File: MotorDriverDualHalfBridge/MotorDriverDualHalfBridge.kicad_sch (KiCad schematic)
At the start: 41 parts, among them J1 Battery Terminal +, J2 Battery Terminal -, J3 Motor Battery Connection, J4 Motor Load Connection, J5 Conn_01x02_Male, J6 Conn_01x02_Male, K1 G8PM, Q1 IAUA250N04S6N005, Q2 IAUA250N04S6N005, Q3 Q_NMOS_DGS, U1 2ED21824S06J, U2 TLI4871

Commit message: PCB V0.1
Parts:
- removed J5, J6: Conn_01x02_Male, Connector_PinHeader_1.27mm:PinHeader_1x02_P1.27mm_Vertical, symbol Connector:Conn_01x02_Male
- added C14: 100uF, Capacitor_SMD:CP_Elec_10x14.3, symbol Device:C_Polarized_Small_US
- added C16, C17, C18, C19, C20: 100uF, Capacitor_SMD:CP_Elec_6.3x5.4_Nichicon, symbol Device:C_Polarized_Small_US
- added HS1: Heatsink_Pad, Library:HSB25-282810, symbol Mechanical:Heatsink_Pad
- added J10: RJ45_LED_Shielded, Connector_RJ:RJ45_Amphenol_RJHSE538X, symbol Connector:RJ45_LED_Shielded
- added J5, J6: Conn_01x04, Connector_JST:JST_EH_B4B-EH-A_1x04_P2.50mm_Vertical, symbol Connector_Generic:Conn_01x04
- added J7: Conn_01x06_Pin, Connector_PinHeader_1.27mm:PinHeader_1x06_P1.27mm_Vertical, symbol Connector:Conn_01x06_Pin
- added NT1: NetTie_2, NetTie:NetTie-2_SMD_Pad2.0mm, symbol Device:NetTie_2
- C13, C6: footprint Capacitor_SMD:CP_Elec_5x4.4 -> Capacitor_SMD:CP_Elec_10x14.3
- F1: footprint Fuse:Fuseholder_Clip-5x20mm_Bel_FC-203-22_Lateral_P17.80x5.00mm_D1.17mm_Horizontal -> Fuse:Fuseholder_Blade_Mini_Keystone_3568
- Q1, Q2: footprint IFX-PG-HSOF-5-1-V:IFX-PG-HSOF-5-1-V -> Library:IAUA250N04S6N005AUMA1
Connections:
- net +12V: now also C20.1, J6.1 (Pin_1), J6.2 (Pin_2)
- net +3.3V: now also C19.1, J5.1 (Pin_1), J5.2 (Pin_2)
- net +BATT: now also C14.1, C16.1, C17.1, C18.1
- net A_{OUT}: now also J10.1, J7.6 (Pin_6)
- net GND: now also C19.2, C20.2, J10.10, J10.12, J10.3, J10.6, J10.SH, J5.3 (Pin_3), J5.4 (Pin_4), J6.3 (Pin_3), J6.4 (Pin_4), NT1.1; no longer C5.2, Q2.1 (S), Q2.2 (S), Q2.3 (S), Q2.4 (S)
- net GNDPWR: now also C5.2, Q2.1 (S), Q2.2 (S), Q2.3 (S), Q2.4 (S), C14.2, NT1.2
- net H_{IN}: now also J10.8, J7.1 (Pin_1)
- net LOAD: now also C16.2, C17.2, C18.2
- net L_{IN}: now also J10.7, J7.2 (Pin_2)
- net OCD_{1}: now also J10.5, J10.9, J7.3 (Pin_3)
- net OCD_{2}: now also J10.11, J10.4, J7.4 (Pin_4)
- net V_{REF}: now also J10.2, J7.5 (Pin_5)
- no-connect marks 0 -> 1
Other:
- moved on the sheet: C1, C13, C2, C3, C4, C5, J3, J4, JP1, Q1, Q2, R1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

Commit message: Updated Schematic
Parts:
- removed C14: 100uF, Capacitor_SMD:CP_Elec_10x14.3, symbol Device:C_Polarized_Small_US
- removed D1: D_TVS, Diode_SMD:D_SMF, symbol Device:D_TVS
- removed J10: RJ45_LED_Shielded, Connector_RJ:RJ45_Amphenol_RJHSE538X, symbol Connector:RJ45_LED_Shielded
- removed J7: Conn_01x06_Pin, Connector_PinHeader_1.27mm:PinHeader_1x06_P1.27mm_Vertical, symbol Connector:Conn_01x06_Pin
- removed K1: G8PM, Library:G8PM1AW7RDC12, symbol MyLibrary:G8PM
- removed Q3: Q_NMOS_DGS, Package_TO_SOT_THT:TO-220F-3_Vertical, symbol Device:Q_NMOS_DGS
- removed R8: 120Ω, Resistor_SMD:R_0603_1608Metric_Pad0.98x0.95mm_HandSolder, symbol Device:R_Small
- added J11, J7, J8: Conn_01x03, Library:MOLEX_2078430003_L1NK_250_3-PIN, symbol Connector_Generic:Conn_01x03
- J5, J6: footprint Connector_JST:JST_EH_B4B-EH-A_1x04_P2.50mm_Vertical -> Library:MOLEX_2078430004_L1NK_250_4-PIN
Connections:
- net +BATT: now also U2.7 (IP-)
- net A_{OUT}: now also J11.2 (Pin_2)
- net GND: now also J11.3 (Pin_3), J7.3 (Pin_3), J8.3 (Pin_3)
- net H_{IN}: now also J8.1 (Pin_1)
- net L_{IN}: now also J8.2 (Pin_2)
- net OCD_{1}: now also J7.1 (Pin_1)
- net OCD_{2}: now also J7.2 (Pin_2)
- net V_{REF}: now also J11.1 (Pin_1)
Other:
- moved on the sheet: C10, C11, C12, C13, C6, C7, C8, C9, F1, J1, J2, R10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

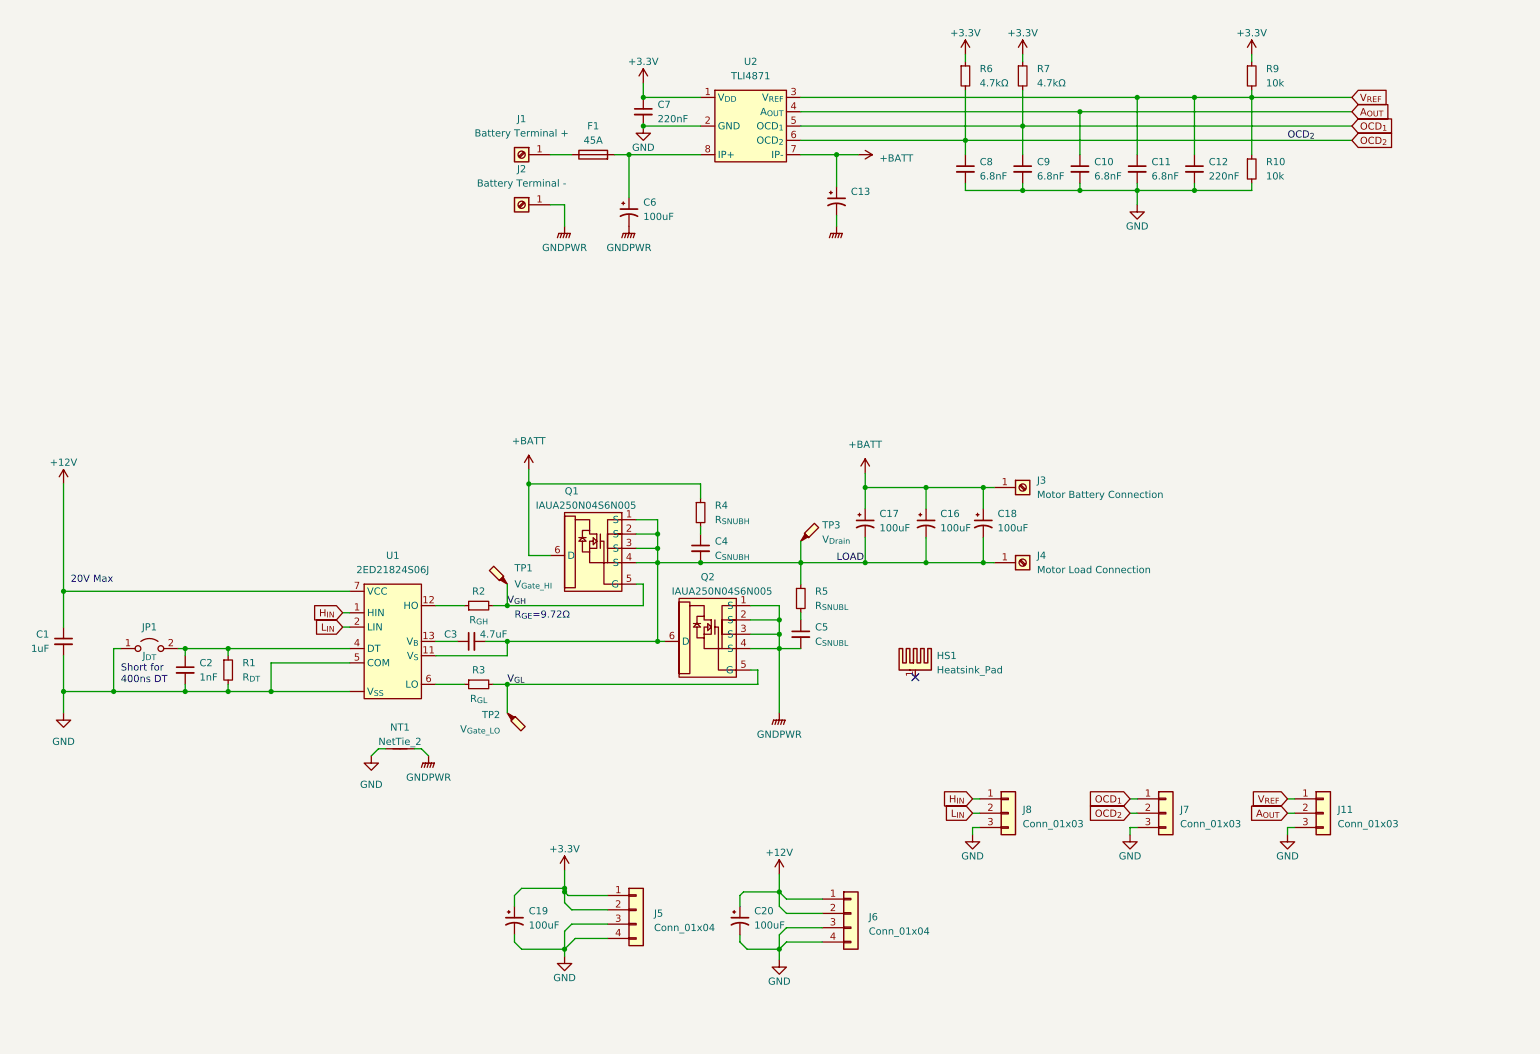
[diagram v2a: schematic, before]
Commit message: Updated Motor Driver Dual Half Bridge
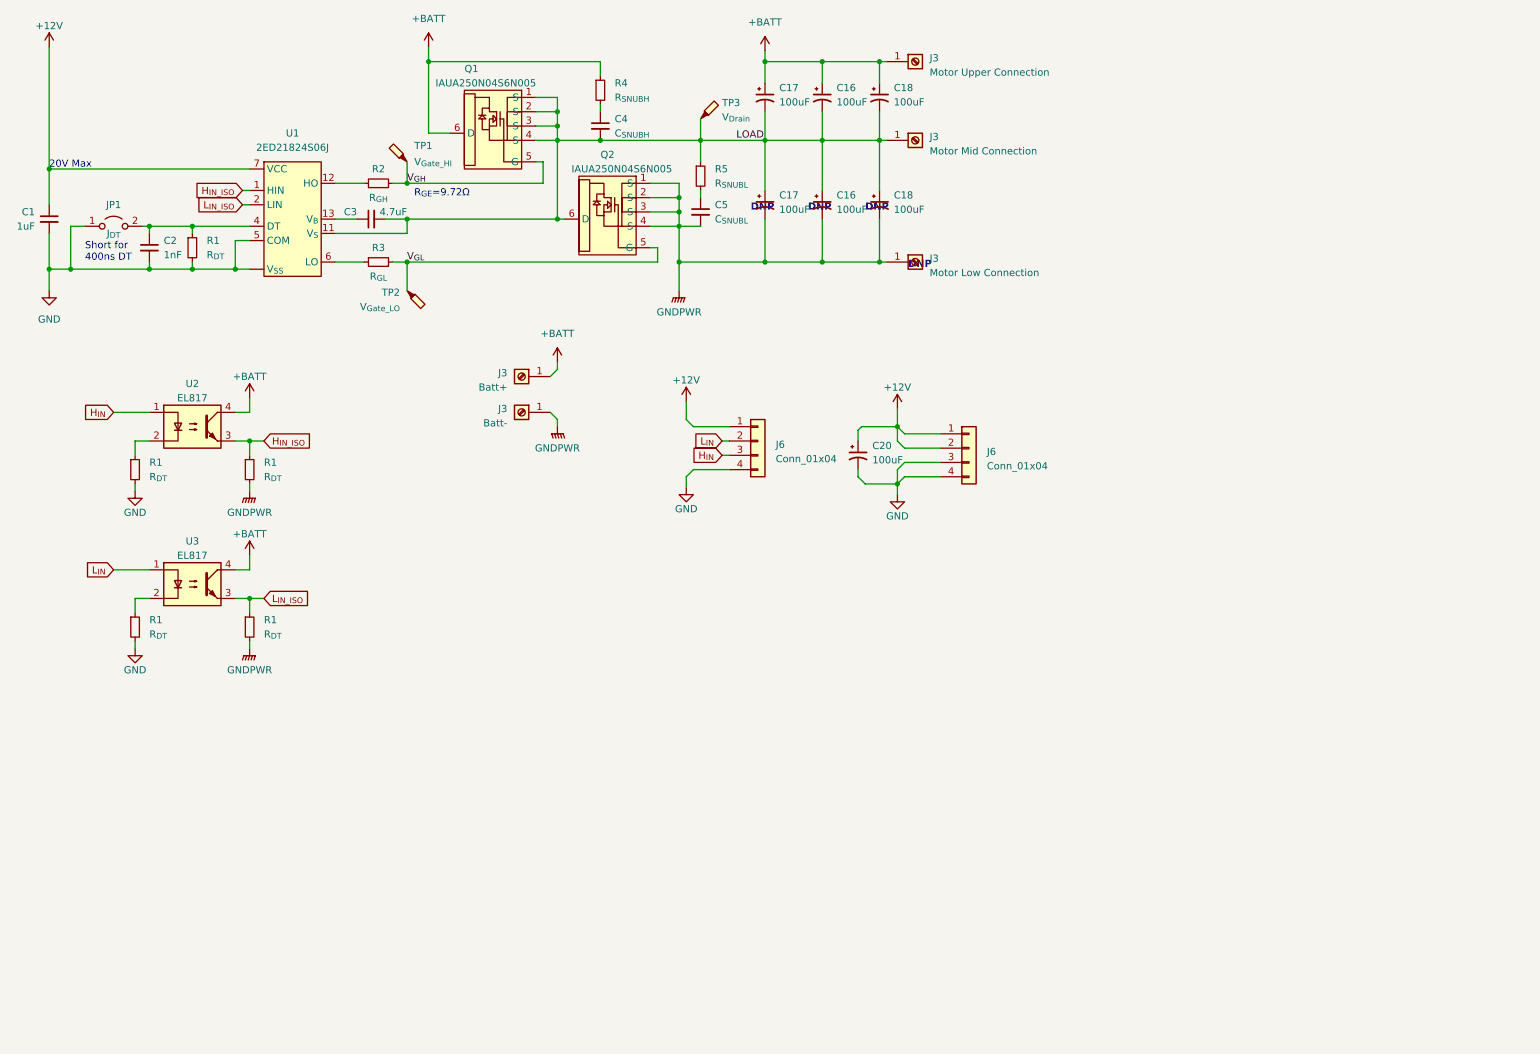
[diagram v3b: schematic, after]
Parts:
- removed C10, C11, C8, C9: 6.8nF, Capacitor_SMD:C_0603_1608Metric_Pad1.08x0.95mm_HandSolder, symbol Device:C_Small
- removed C12, C7: 220nF, Capacitor_SMD:C_0603_1608Metric_Pad1.08x0.95mm_HandSolder, symbol Device:C_Small
- removed C13, C6: 100uF, Capacitor_SMD:CP_Elec_10x14.3, symbol Device:C_Polarized_Small_US
- removed C19: 100uF, Capacitor_SMD:CP_Elec_6.3x5.4_Nichicon, symbol Device:C_Polarized_Small_US
- removed F1: 45A, Fuse:Fuseholder_Blade_Mini_Keystone_3568, symbol Device:Fuse
- removed HS1: Heatsink_Pad, Library:HSB25-282810, symbol Mechanical:Heatsink_Pad
- removed J1: Battery Terminal +, Library:74651195R, symbol Connector:Screw_Terminal_01x01
- removed J11, J7, J8: Conn_01x03, Library:MOLEX_2078430003_L1NK_250_3-PIN, symbol Connector_Generic:Conn_01x03
- removed J2: Battery Terminal -, Library:74651195R, symbol Connector:Screw_Terminal_01x01
- removed J4: Motor Load Connection, Library:74651195R, symbol Connector:Screw_Terminal_01x01
- removed J5: Conn_01x04, Library:MOLEX_2078430004_L1NK_250_4-PIN, symbol Connector_Generic:Conn_01x04
- removed NT1: NetTie_2, NetTie:NetTie-2_SMD_Pad2.0mm, symbol Device:NetTie_2
- removed R10, R9: 10k, Resistor_SMD:R_0603_1608Metric_Pad0.98x0.95mm_HandSolder, symbol Device:R_Small
- removed R6, R7: 4.7kΩ, Resistor_SMD:R_0603_1608Metric_Pad0.98x0.95mm_HandSolder, symbol Device:R_Small
- removed U2: TLI4871, Library:TLI4971A120T5E0001XUMA1, symbol MyLibrary:TLI4871
- added C16, C17, C18: 100uF, Capacitor_SMD:CP_Elec_6.3x5.4_Nichicon, symbol Device:C_Polarized_Small_US
- added J3: Batt-, TerminalBlock_Wuerth:Wuerth_REDCUBE-THR_WP-THRBU_74650194_THR, symbol Connector:Screw_Terminal_01x01
- added J3: Motor Mid Connection, TerminalBlock_Wuerth:Wuerth_REDCUBE-THR_WP-THRBU_74650194_THR, symbol Connector:Screw_Terminal_01x01
- added J3: Batt+, TerminalBlock_Wuerth:Wuerth_REDCUBE-THR_WP-THRBU_74650194_THR, symbol Connector:Screw_Terminal_01x01
- added J3: Motor Low Connection, TerminalBlock_Wuerth:Wuerth_REDCUBE-THR_WP-THRBU_74650194_THR, symbol Connector:Screw_Terminal_01x01
- added J6: Conn_01x04, Library:MOLEX_2078430004_L1NK_250_4-PIN, symbol Connector_Generic:Conn_01x04
- added R1 (x4): R_{DT}, Resistor_THT:R_Axial_DIN0207_L6.3mm_D2.5mm_P10.16mm_Horizontal, symbol Device:R_Small
- added U2, U3: EL817, Package_DIP:DIP-4_W7.62mm, symbol Isolator:EL817
- J3: value Motor Battery Connection -> Motor Upper Connection; footprint Library:74651195R -> TerminalBlock_Wuerth:Wuerth_REDCUBE-THR_WP-THRBU_74650194_THR
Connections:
- net +12V: now also J6.1 (Pin_1)
- net +BATT: now also J3.1 (Pin_1), U2.4, U3.4
- net GND: now also J6.4 (Pin_4), R1.2, R1.2
- net GNDPWR: now also C16.2, C17.2, C18.2, J3.1 (Pin_1), J3.1 (Pin_1), R1.2, R1.2
- net H_{IN}: now also J6.3 (Pin_3), U2.1; no longer U1.1 (HIN)
- net LOAD: now also C16.1, C17.1, C18.1, J3.1 (Pin_1)
- net L_{IN}: now also J6.2 (Pin_2), U3.1; no longer U1.2 (LIN)
- new net: R1.1, U2.2
- new net: R1.1, U3.2
- new net H_{IN}_{_ISO}: R1.1, U1.1 (HIN), U2.3
- new net L_{IN}_{_ISO}: R1.1, U1.2 (LIN), U3.3
- no-connect marks 1 -> 0
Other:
- note added: "DNP"
- moved on the sheet: C1, C16, C17, C18, C2, C20, C3, C4, C5, J3, J6, JP1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

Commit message: Motor Driver V1.0
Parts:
- removed J3: Batt-, TerminalBlock_Wuerth:Wuerth_REDCUBE-THR_WP-THRBU_74650194_THR, symbol Connector:Screw_Terminal_01x01
- removed J3: Motor Mid Connection, TerminalBlock_Wuerth:Wuerth_REDCUBE-THR_WP-THRBU_74650194_THR, symbol Connector:Screw_Terminal_01x01
- removed J3: Batt+, TerminalBlock_Wuerth:Wuerth_REDCUBE-THR_WP-THRBU_74650194_THR, symbol Connector:Screw_Terminal_01x01
- removed J3: Motor Low Connection, TerminalBlock_Wuerth:Wuerth_REDCUBE-THR_WP-THRBU_74650194_THR, symbol Connector:Screw_Terminal_01x01
- added H1, H2, H3, H4, H5: MountingHole_Pad, MountingHole:MountingHole_2.5mm_Pad, symbol Mechanical:MountingHole_Pad
- added J3: Motor Bottom Connection, Library:M5 Screw Terminal, symbol Connector:Screw_Terminal_01x01
- added J3: Batt-, Library:M5 Screw Terminal, symbol Connector:Screw_Terminal_01x01
- added J3: Motor Middle Connection, Library:M5 Screw Terminal, symbol Connector:Screw_Terminal_01x01
- added J3: Batt+, Library:M5 Screw Terminal, symbol Connector:Screw_Terminal_01x01
- C16, C17, C18: value 100uF -> 100nF; now not fitted
- C16, C17, C18: value 100uF -> 100nF
- C4, C5: footprint Capacitor_SMD:C_0603_1608Metric_Pad1.08x0.95mm_HandSolder -> Capacitor_SMD:C_0805_2012Metric_Pad1.18x1.45mm_HandSolder
- J3: footprint TerminalBlock_Wuerth:Wuerth_REDCUBE-THR_WP-THRBU_74650194_THR -> Library:M5 Screw Terminal
- R2, R3, R4, R5: footprint Resistor_SMD:R_0603_1608Metric_Pad0.98x0.95mm_HandSolder -> Resistor_SMD:R_0805_2012Metric_Pad1.20x1.40mm_HandSolder
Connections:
- net +BATT: now also J3.10 (e), J3.11, J3.12, J3.13, J3.14 (e), J3.15 (Pin_1), J3.16 (Pin_1), J3.2, J3.3, J3.4, J3.5, J3.6 (e), J3.7, J3.8, J3.9, J3.1 (Pin_1), J3.10 (e), J3.11, J3.12, J3.13, J3.14 (e), J3.15 (Pin_1), J3.16 (Pin_1), J3.2, J3.3, J3.4, J3.5, J3.6 (e), J3.7, J3.8, J3.9
- net GNDPWR: now also J3.1 (Pin_1), J3.1 (Pin_1), J3.10 (e), J3.10 (e), J3.11, J3.11, J3.12, J3.12, J3.13, J3.13, J3.14 (e), J3.14 (e), J3.15 (Pin_1), J3.15 (Pin_1), J3.16 (Pin_1), J3.16 (Pin_1), J3.2, J3.2, J3.3, J3.3, J3.4, J3.4, J3.5, J3.5, J3.6 (e), J3.6 (e), J3.7, J3.7, J3.8, J3.8, J3.9, J3.9
- net LOAD: now also J3.1 (Pin_1), J3.10 (e), J3.11, J3.12, J3.13, J3.14 (e), J3.15 (Pin_1), J3.16 (Pin_1), J3.2, J3.3, J3.4, J3.5, J3.6 (e), J3.7, J3.8, J3.9
- new net Earth_Clean: H1.1, H2.1, H3.1, H4.1, H5.1
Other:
- note removed: "DNP"

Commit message: Motor Driver V1.01
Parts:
- removed C20: 100uF, Capacitor_SMD:CP_Elec_6.3x5.4_Nichicon, symbol Device:C_Polarized_Small_US
- removed J3: Motor Bottom Connection, Library:M5 Screw Terminal, symbol Connector:Screw_Terminal_01x01
- removed J3: Motor Upper Connection, Library:M5 Screw Terminal, symbol Connector:Screw_Terminal_01x01
- removed J3: Batt-, Library:M5 Screw Terminal, symbol Connector:Screw_Terminal_01x01
- removed J3: Motor Middle Connection, Library:M5 Screw Terminal, symbol Connector:Screw_Terminal_01x01
- removed J3: Batt+, Library:M5 Screw Terminal, symbol Connector:Screw_Terminal_01x01
- removed J6 (x2): Conn_01x04, Library:MOLEX_2078430004_L1NK_250_4-PIN, symbol Connector_Generic:Conn_01x04
- removed Q1, Q2: IAUA250N04S6N005, Library:IAUA250N04S6N005AUMA1, symbol MySymbols:IAUA250N04S6N005
- removed R1 (x4): R_{DT}, Resistor_THT:R_Axial_DIN0207_L6.3mm_D2.5mm_P10.16mm_Horizontal, symbol Device:R_Small
- removed TP1: V_{Gate_HI}, TestPoint:TestPoint_Pad_D1.0mm, symbol Connector:TestPoint_Probe
- removed TP2: V_{Gate_LO}, TestPoint:TestPoint_Pad_D1.0mm, symbol Connector:TestPoint_Probe
- removed TP3: V_{Drain}, TestPoint:TestPoint_Pad_D1.0mm, symbol Connector:TestPoint_Probe
- removed U2, U3: EL817, Package_DIP:DIP-4_W7.62mm, symbol Isolator:EL817
- added C1: 0.1uF, Capacitor_SMD:C_0603_1608Metric_Pad1.08x0.95mm_HandSolder, symbol Device:C_Small
- added C1: 100uF, Capacitor_SMD:C_Elec_5x5.8, symbol Device:C_Small
- added C1: 22uF, Capacitor_SMD:CP_Elec_5x5.8, symbol Device:C_Small
- added J1, J4, J5: ~, symbol My Global Library:M5_Screw_Terminal_Side
- added J2, J3: ~, symbol My Global Library:M5 Screw Terminal Both
- added J7: Conn_01x02, Connector_JST:JST_EH_B2B-EH-A_1x02_P2.50mm_Vertical, symbol Connector_Generic:Conn_01x02
- added Q1, Q2: NMOS, symbol Simulation_SPICE:NMOS
- added R1: 1k, Resistor_THT:R_Axial_DIN0207_L6.3mm_D2.5mm_P10.16mm_Horizontal, symbol Device:R_Small
- added R1: 4.7k, Resistor_THT:R_Axial_DIN0207_L6.3mm_D2.5mm_P10.16mm_Horizontal, symbol Device:R_Small
- added R1: 1.8k, Resistor_THT:R_Axial_DIN0207_L6.3mm_D2.5mm_P10.16mm_Horizontal, symbol Device:R_Small
- added R2 (x2): 1Μ, Resistor_SMD:R_0805_2012Metric_Pad1.20x1.40mm_HandSolder, symbol Device:R_Small
- added U2: ~, Library:I3A4W005A150V001R, symbol SymbolLibrary:U?
- added U4: LM358, Package_DIP:DIP-8_W7.62mm_LongPads, symbol Amplifier_Operational:LM358
- added U5: EL817, Package_DIP:DIP-4_W7.62mm, symbol Isolator:EL817
- C1, C2, C4, C5, R1, R4, R5: now not fitted
- R2: value R_{G}_{H} -> 3.3Ω
- R3: value R_{G}_{L} -> 3.3Ω
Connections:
- net GND is gone; now on net GNDPWR: C1.2, C2.2, JP1.1 (A), R1.2, U1. (V_{SS}), U1.5 (COM)
- net H_{IN}_{_ISO} is gone; now on net H_{IN}: U1.1 (HIN)
- net L_{IN}_{_ISO} is gone; now on net L_{IN}: U1.2 (LIN)
- net +BATT: now also C1.1, J3.1 (0), Q1.1 (D), U2.1 (V_{IN+})
- net GNDPWR: now also C1.2, C1.2, C1.2, J2.1 (0), Q2.3 (S), R1.1, R1.2, R2.2, U2.2 (ON/OFF), U2.3 (V_{IN-}), U2.4 (V_{OUT}-), U4.3 (+), U4.4 (V-), U4.6 (-)
- net H_{IN}: now also U4.1
- net LOAD: now also J1.1 (0), Q1.3 (S), Q2.1 (D), R2.2
- net L_{IN}: now also U4.7
- net V_{GH}: now also Q1.2 (G), R2.1
- net V_{GL}: now also Q2.2 (G), R2.1
- net +12V renamed VDD
- net VDD: now also C1.1, C1.1, U2.7 (SENSE), U2.8 (V_{OUT}+), U4.8 (V+), U5.4
- new net: R1.1, U4.2 (-), U4.5 (+), U5.3
- new net: J7.1 (Pin_1), R1.1
- new net: J7.2 (Pin_2), U5.2
- new net: R1.2, U5.1
- new net: J2.1 (0), J5.1 (0)
- new net: J3.1 (0), J4.1 (0)
- new net: R1.2, U2.6 (TRIM)
- no-connect marks 0 -> 1
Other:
- note added: "12V Power Supply"
- note added: "Battery Negative Connector"
- note added: "Battery Positive Connection"
- note added: "Filtering Capacitors"
- note added: "Motor Bot"
- note added: "Motor Driver"
- note added: "Motor Mid"
- note added: "Motor Top"
- note added: "Mounting Holes"
- note added: "Signal Spliter & Inverter"
- note added: "Snubber Circuit"
- note removed: "20V Max"
- note removed: "R_{GE}=9.72Ω"
- moved on the sheet: C3, JP1, R2, R3, U1
